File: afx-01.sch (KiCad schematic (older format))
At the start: 25 parts, among them P1 CONN_02X05, P2 CONN_02X08, Q5 BSS138, Q6 BSS138, U1 ADA_SSD1306_I2C, U10 MicroSD_Connector, U2 Teensy_3.1, U4 MicroSD_Adapter, U5 MCP1703

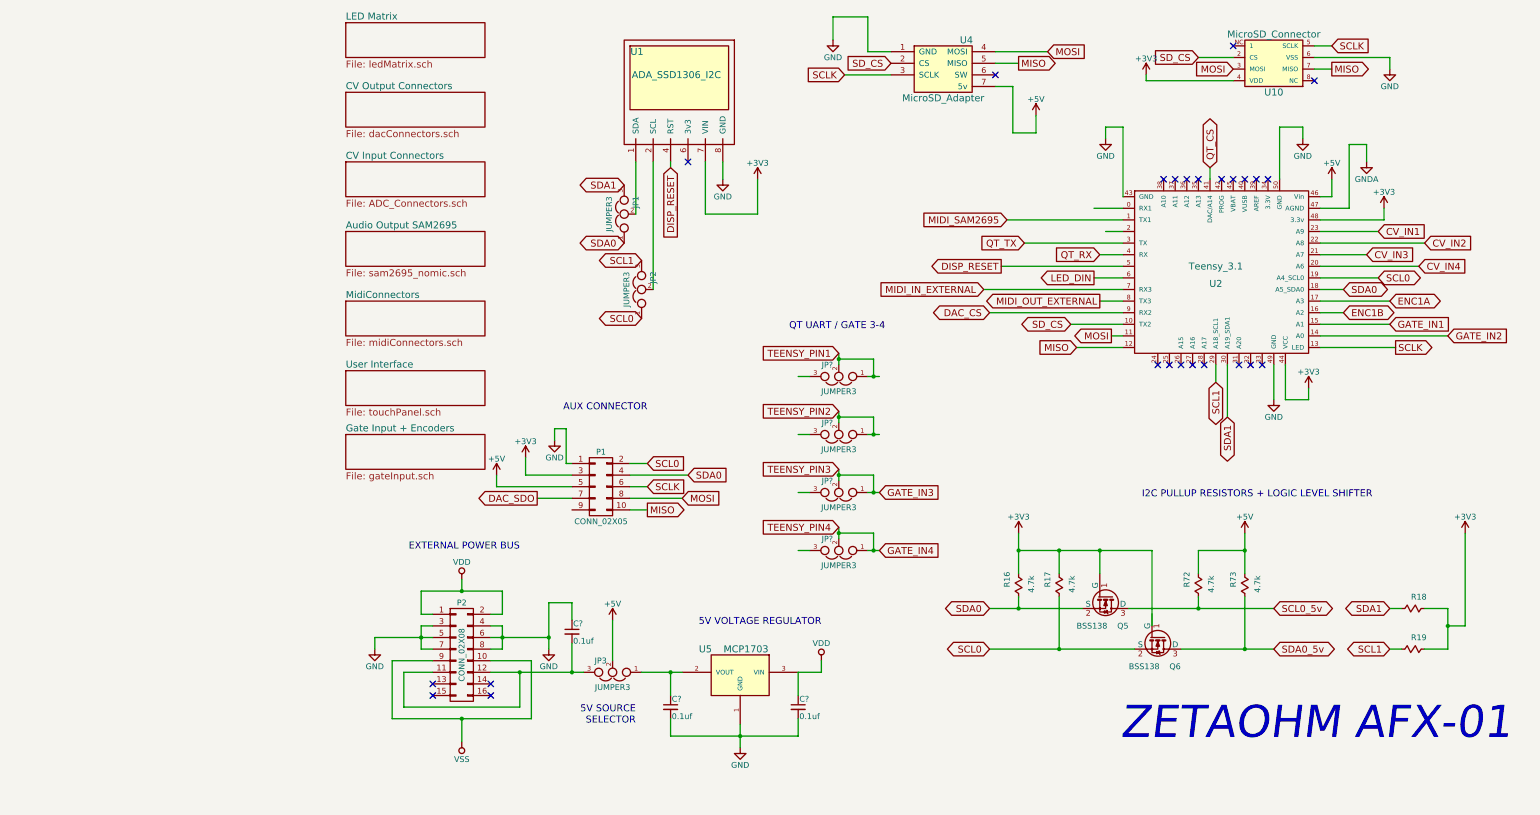
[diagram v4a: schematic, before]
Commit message: Updating footprints
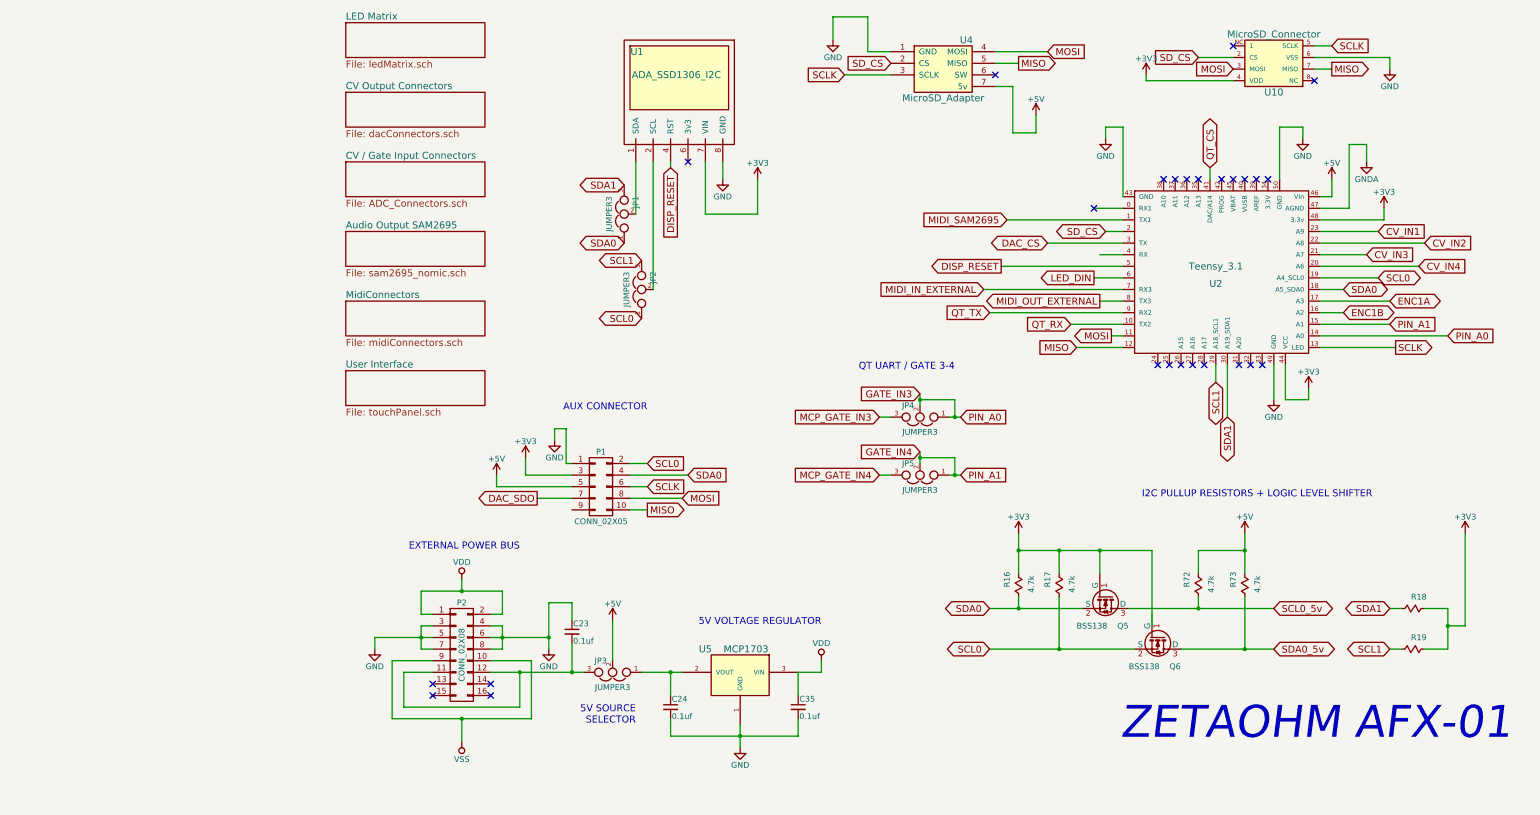
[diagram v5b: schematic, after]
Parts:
- removed JP? (x2): JUMPER3, Zetaohm:Jumper_3way, symbol JUMPER3
- C23, C24, C35: renamed from C?; footprint (none) -> Capacitors_SMD:C_0603_HandSoldering
- R16, R17, R18, R19, R72, R73: footprint Resistors_SMD:R_0805_HandSoldering -> Resistors_SMD:R_0603_HandSoldering
- U1: footprint Zetaohm:SSD1306 -> Pin_Headers:Pin_Header_Angled_1x06
- gave numbers to parts that had none: 2
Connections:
- net labels added: MCP_GATE_IN3, MCP_GATE_IN4, PIN_A0, PIN_A1
- net labels removed: GATE_IN1, GATE_IN2, TEENSY_PIN1, TEENSY_PIN2, TEENSY_PIN3, TEENSY_PIN4
- wire segments 168 -> 158
- no-connect marks 25 -> 26
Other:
- moved on the sheet: JP4, JP5
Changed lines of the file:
@@
 $Descr A4 11693 8268
 encoding utf-8
-Sheet 1 8
+Sheet 1 7
 Title ""
 Date ""
@@
 F 0 "R16" V 6900 5600 50  0000 C CNN
 F 1 "4.7k" V 6690 5640 50  0000 C CNN
-F 2 "Resistors_SMD:R_0805_HandSoldering" V 6730 5650 30  0001 C CNN
+F 2 "Resistors_SMD:R_0603_HandSoldering" V 6730 5650 30  0001 C CNN
 F 3 "" H 6800 5640 30  0000 C CNN
 	1    6800 5650
@@
 F 0 "R17" V 7250 5600 50  0000 C CNN
 F 1 "4.7k" V 7040 5640 50  0000 C CNN
-F 2 "Resistors_SMD:R_0805_HandSoldering" V 7080 5650 30  0001 C CNN
+F 2 "Resistors_SMD:R_0603_HandSoldering" V 7080 5650 30  0001 C CNN
 F 3 "" H 7150 5640 30  0000 C CNN
 	1    7150 5650
@@
 F 0 "R19" V 10300 6150 50  0000 C CNN
 F 1 "4.7k" V 10090 6190 50  0001 C CNN
-F 2 "Resistors_SMD:R_0805_HandSoldering" V 10130 6200 30  0001 C CNN
+F 2 "Resistors_SMD:R_0603_HandSoldering" V 10130 6200 30  0001 C CNN
 F 3 "" H 10200 6190 30  0000 C CNN
 	1    10200 6200
@@
 F 0 "R18" V 10300 5800 50  0000 C CNN
 F 1 "4.7k" V 10090 5840 50  0001 C CNN
-F 2 "Resistors_SMD:R_0805_HandSoldering" V 10130 5850 30  0001 C CNN
+F 2 "Resistors_SMD:R_0603_HandSoldering" V 10130 5850 30  0001 C CNN
 F 3 "" H 10200 5840 30  0000 C CNN
 	1    10200 5850
@@
 F 0 "U1" H 3510 2150 60  0000 C CNN
 F 1 "ADA_SSD1306_I2C" H 3850 1950 60  0000 C CNN
-F 2 "Zetaohm:SSD1306" V 4050 1550 60  0001 C CNN
+F 2 "Pin_Headers:Pin_Header_Angled_1x06" V 4050 1550 60  0001 C CNN
 F 3 "" V 4050 1550 60  0000 C CNN
 	1    3850 1600
@@
 	1    0    0    -1
 $EndComp
-Text GLabel 6550 3300 0    60   3State ~ 0
+Text GLabel 7050 2700 0    60   3State ~ 0
 DAC_CS
 Text GLabel 10050 3600 2    60   Output ~ 0
@@
 Text GLabel 7300 3600 0    60   Input ~ 0
 MISO
-Text GLabel 7250 3400 0    60   3State ~ 0
+Text GLabel 7550 2600 0    60   3State ~ 0
 SD_CS
 Text GLabel 5300 1250 0    60   Input ~ 0
@@
 S 1000 2000 1200 300
 U 561FE26C
-F0 "CV Input Connectors" 60
+F0 "CV / Gate Input Connectors" 60
 F1 "ADC_Connectors.sch" 60
 $EndSheet
@@
 Text GLabel 10250 2900 2    60   Input ~ 0
 CV_IN4
-Text GLabel 10000 3400 2    60   Input ~ 0
-GATE_IN1
-Text GLabel 10500 3500 2    60   Input ~ 0
-GATE_IN2
 NoConn ~ 8200 3750
 NoConn ~ 8100 3750
@@
 F 0 "R72" V 8450 5600 50  0000 C CNN
 F 1 "4.7k" V 8240 5640 50  0000 C CNN
-F 2 "Resistors_SMD:R_0805_HandSoldering" V 8280 5650 30  0001 C CNN
+F 2 "Resistors_SMD:R_0603_HandSoldering" V 8280 5650 30  0001 C CNN
 F 3 "" H 8350 5640 30  0000 C CNN
 	1    8350 5650
@@
 F 0 "R73" V 8850 5600 50  0000 C CNN
 F 1 "4.7k" V 8640 5640 50  0000 C CNN
-F 2 "Resistors_SMD:R_0805_HandSoldering" V 8680 5650 30  0001 C CNN
+F 2 "Resistors_SMD:R_0603_HandSoldering" V 8680 5650 30  0001 C CNN
 F 3 "" H 8750 5640 30  0000 C CNN
 	1    8750 5650
@@
 NoConn ~ 9350 1300
 $Comp
-L C_Small C?
+L C_Small C24
 U 1 1 5628B983
 P 3800 6700
-F 0 "C?" H 3810 6770 50  0000 L CNN
+F 0 "C24" H 3810 6770 50  0000 L CNN
 F 1 "0.1uf" H 3810 6620 50  0000 L CNN
-F 2 "" H 3800 6700 60  0000 C CNN
+F 2 "Capacitors_SMD:C_0603_HandSoldering" H 3800 6700 60  0001 C CNN
 F 3 "" H 3800 6700 60  0000 C CNN
 	1    3800 6700
@@
 $EndComp
 $Comp
-L C_Small C?
+L C_Small C35
 U 1 1 5628BCAF
 P 4900 6700
-F 0 "C?" H 4910 6770 50  0000 L CNN
+F 0 "C35" H 4910 6770 50  0000 L CNN
 F 1 "0.1uf" H 4910 6620 50  0000 L CNN
-F 2 "" H 4900 6700 60  0000 C CNN
+F 2 "Capacitors_SMD:C_0603_HandSoldering" H 4900 6700 60  0001 C CNN
 F 3 "" H 4900 6700 60  0000 C CNN
 	1    4900 6700
@@
 $EndComp
 $Comp
-L C_Small C?
+L C_Small C23
 U 1 1 5628C134
 P 2950 6050
-F 0 "C?" H 2960 6120 50  0000 L CNN
+F 0 "C23" H 2960 6120 50  0000 L CNN
 F 1 "0.1uf" H 2960 5970 50  0000 L CNN
-F 2 "" H 2950 6050 60  0000 C CNN
+F 2 "Capacitors_SMD:C_0603_HandSoldering" H 2950 6050 60  0001 C CNN
 F 3 "" H 2950 6050 60  0000 C CNN
 	1    2950 6050
@@
 Text GLabel 8450 2050 1    60   3State ~ 0
 QT_CS
-Text GLabel 5600 4850 2    60   Input ~ 0
+Text GLabel 5950 4000 0    60   Input ~ 0
 GATE_IN3
-Text GLabel 5600 5350 2    60   Input ~ 0
+Text GLabel 5950 4500 0    60   Input ~ 0
 GATE_IN4
-Text GLabel 7500 2800 0    60   Input ~ 0
+Text GLabel 7250 3400 0    60   Input ~ 0
 QT_RX
-Text GLabel 6850 2700 0    60   Input ~ 0
+Text GLabel 6550 3300 0    60   Input ~ 0
 QT_TX
 $Comp
-L JUMPER3 JP?
+L JUMPER3 JP4
 U 1 1 5629034F
-P 5250 4850
-F 0 "JP?" H 5300 4750 50  0000 L CNN
-F 1 "JUMPER3" H 5250 4950 50  0000 C BNN
-F 2 "Zetaohm:Jumper_3way" H 5250 4850 60  0001 C CNN
-F 3 "" H 5250 4850 60  0000 C CNN
-	1    5250 4850
+P 5950 4200
+F 0 "JP4" H 6000 4100 50  0000 L CNN
+F 1 "JUMPER3" H 5950 4300 50  0000 C BNN
+F 2 "Zetaohm:Jumper_3way" H 5950 4200 60  0001 C CNN
+F 3 "" H 5950 4200 60  0000 C CNN
+	1    5950 4200
 	-1   0    0    1
 $EndComp
 $Comp
-L JUMPER3 JP?
+L JUMPER3 JP5
 U 1 1 5629077E
-P 5250 5350
-F 0 "JP?" H 5300 5250 50  0000 L CNN
-F 1 "JUMPER3" H 5250 5450 50  0000 C BNN
-F 2 "Zetaohm:Jumper_3way" H 5250 5350 60  0001 C CNN
-F 3 "" H 5250 5350 60  0000 C CNN
-	1    5250 5350
+P 5950 4700
+F 0 "JP5" H 6000 4600 50  0000 L CNN
+F 1 "JUMPER3" H 5950 4800 50  0000 C BNN
+F 2 "Zetaohm:Jumper_3way" H 5950 4700 60  0001 C CNN
+F 3 "" H 5950 4700 60  0000 C CNN
+	1    5950 4700
 	-1   0    0    1
 $EndComp
-Text Notes 5650 3450 2    60   ~ 0
+Text Notes 6250 3800 2    60   ~ 0
 QT UART / GATE 3-4
-Text GLabel 5250 4650 0    60   Input ~ 0
-TEENSY_PIN3
-Text GLabel 5250 5150 0    60   Input ~ 0
-TEENSY_PIN4
-$Comp
-L JUMPER3 JP?
-U 1 1 562946F5
-P 5250 3850
-F 0 "JP?" H 5300 3750 50  0000 L CNN
-F 1 "JUMPER3" H 5250 3950 50  0000 C BNN
-F 2 "Zetaohm:Jumper_3way" H 5250 3850 60  0001 C CNN
-F 3 "" H 5250 3850 60  0000 C CNN
-	1    5250 3850
-	-1   0    0    1
-$EndComp
-$Comp
-L JUMPER3 JP?
-U 1 1 562946FB
-P 5250 4350
-F 0 "JP?" H 5300 4250 50  0000 L CNN
-F 1 "JUMPER3" H 5250 4450 50  0000 C BNN
-F 2 "Zetaohm:Jumper_3way" H 5250 4350 60  0001 C CNN
-F 3 "" H 5250 4350 60  0000 C CNN
-	1    5250 4350
-	-1   0    0    1
-$EndComp
-Text GLabel 5250 3650 0    60   Input ~ 0
-TEENSY_PIN1
-Text GLabel 5250 4150 0    60   Input ~ 0
-TEENSY_PIN2
 Wire Wire Line
 	9400 3200 10000 3200
@@
 	7550 2600 7700 2600
 Wire Wire Line
-	7700 2700 6850 2700
+	7700 2700 7050 2700
 Wire Wire Line
 	7500 2800 7700 2800
@@
 Connection ~ 2750 6100
 Wire Wire Line
-	4900 4850 5000 4850
-Wire Wire Line
-	5250 4650 5250 4750
-Wire Wire Line
-	5500 4850 5600 4850
-Wire Wire Line
-	5500 5350 5600 5350
-Wire Wire Line
-	5000 5350 4900 5350
-Wire Wire Line
-	5250 5150 5250 5250
-Wire Wire Line
-	4900 3850 5000 3850
-Wire Wire Line
-	5250 3650 5250 3750
-Wire Wire Line
-	5500 3850 5600 3850
-Wire Wire Line
-	5500 4350 5600 4350
-Wire Wire Line
-	5000 4350 4900 4350
-Wire Wire Line
-	5250 4150 5250 4250
-Wire Wire Line
-	5250 3700 5550 3700
-Wire Wire Line
-	5550 3700 5550 3850
-Connection ~ 5550 3850
-Connection ~ 5250 3700
-Wire Wire Line
-	5250 4200 5550 4200
-Wire Wire Line
-	5550 4200 5550 4350
-Connection ~ 5550 4350
-Connection ~ 5250 4200
-Wire Wire Line
-	5250 4700 5550 4700
-Wire Wire Line
-	5550 4700 5550 4850
-Connection ~ 5550 4850
-Connection ~ 5250 4700
-Wire Wire Line
-	5250 5200 5550 5200
-Wire Wire Line
-	5550 5200 5550 5350
-Connection ~ 5550 5350
-Connection ~ 5250 5200
-$Sheet
-S 1000 4350 1200 300
-U 56295FCA
-F0 "Gate Input + Encoders" 60
-F1 "gateInput.sch" 60
-$EndSheet
+	5600 4200 5700 4200
+Wire Wire Line
+	5950 4000 5950 4100
+Wire Wire Line
+	6200 4200 6300 4200
+Wire Wire Line
+	6200 4700 6300 4700
+Wire Wire Line
+	5700 4700 5600 4700
+Wire Wire Line
+	5950 4500 5950 4600
+Wire Wire Line
+	5950 4050 6250 4050
+Wire Wire Line
+	6250 4050 6250 4200
+Connection ~ 6250 4200
+Connection ~ 5950 4050
+Wire Wire Line
+	5950 4550 6250 4550
+Wire Wire Line
+	6250 4550 6250 4700
+Connection ~ 6250 4700
+Connection ~ 5950 4550
+Text GLabel 10000 3400 2    60   Input ~ 0
+PIN_A1
+Text GLabel 10500 3500 2    60   Input ~ 0
+PIN_A0
+Text GLabel 6300 4200 2    60   Input ~ 0
+PIN_A0
+Text GLabel 6300 4700 2    60   Input ~ 0
+PIN_A1
+Text GLabel 5600 4200 0    60   Input ~ 0
+MCP_GATE_IN3
+Text GLabel 5600 4700 0    60   Input ~ 0
+MCP_GATE_IN4
+NoConn ~ 7450 2400
 $EndSCHEMATC

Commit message: Populating pcb file
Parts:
- removed JP4, JP5: JUMPER3, Zetaohm:Jumper_3way, symbol JUMPER3
- P2: footprint Pin_Headers:Pin_Header_Angled_2x08 -> Pin_Headers:Pin_Header_Straight_2x08
- U1: footprint Pin_Headers:Pin_Header_Angled_1x06 -> Pin_Headers:Pin_Header_Straight_1x06
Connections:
- net GATE_IN3 renamed PIN_A0
- net GATE_IN4 renamed PIN_A1
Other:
- note removed: "QT UART / GATE 3-4"
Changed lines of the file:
@@
 F 0 "U1" H 3510 2150 60  0000 C CNN
 F 1 "ADA_SSD1306_I2C" H 3850 1950 60  0000 C CNN
-F 2 "Pin_Headers:Pin_Header_Angled_1x06" V 4050 1550 60  0001 C CNN
+F 2 "Pin_Headers:Pin_Header_Straight_1x06" V 4050 1550 60  0001 C CNN
 F 3 "" V 4050 1550 60  0000 C CNN
 	1    3850 1600
@@
 SD_CS
 $Comp
-L +3V3 #PWR01
+L +3V3 #PWR17
 U 1 1 561E6C12
 P 6800 5200
-F 0 "#PWR01" H 6800 5050 50  0001 C CNN
+F 0 "#PWR17" H 6800 5050 50  0001 C CNN
 F 1 "+3V3" H 6800 5340 50  0000 C CNN
 F 2 "" H 6800 5200 60  0000 C CNN
@@
 SCL1
 $Comp
-L +3V3 #PWR02
+L +3V3 #PWR19
 U 1 1 561E70C9
 P 10650 5200
-F 0 "#PWR02" H 10650 5050 50  0001 C CNN
+F 0 "#PWR19" H 10650 5050 50  0001 C CNN
 F 1 "+3V3" H 10650 5340 50  0000 C CNN
 F 2 "" H 10650 5200 60  0000 C CNN
@@
 ENC1B
 $Comp
-L +3V3 #PWR03
+L +3V3 #PWR12
 U 1 1 561E88DC
 P 9300 3950
-F 0 "#PWR03" H 9300 3800 50  0001 C CNN
+F 0 "#PWR12" H 9300 3800 50  0001 C CNN
 F 1 "+3V3" H 9300 4090 50  0000 C CNN
 F 2 "" H 9300 3950 60  0000 C CNN
@@
 $EndComp
 $Comp
-L GND #PWR04
+L GND #PWR13
 U 1 1 561E894C
 P 9000 4050
-F 0 "#PWR04" H 9000 3800 50  0001 C CNN
+F 0 "#PWR13" H 9000 3800 50  0001 C CNN
 F 1 "GND" H 9000 3900 50  0000 C CNN
 F 2 "" H 9000 4050 60  0000 C CNN
@@
 $EndComp
 $Comp
-L +5V #PWR05
+L +5V #PWR10
 U 1 1 561E8C0A
 P 9500 2150
-F 0 "#PWR05" H 9500 2000 50  0001 C CNN
+F 0 "#PWR10" H 9500 2000 50  0001 C CNN
 F 1 "+5V" H 9500 2290 50  0000 C CNN
 F 2 "" H 9500 2150 60  0000 C CNN
@@
 $EndComp
 $Comp
-L +3V3 #PWR06
+L +3V3 #PWR11
 U 1 1 561E8F33
 P 9950 2400
-F 0 "#PWR06" H 9950 2250 50  0001 C CNN
+F 0 "#PWR11" H 9950 2250 50  0001 C CNN
 F 1 "+3V3" H 9950 2540 50  0000 C CNN
 F 2 "" H 9950 2400 60  0000 C CNN
@@
 $EndComp
 $Comp
-L GNDA #PWR07
+L GNDA #PWR7
 U 1 1 561E8FA3
 P 9800 2000
-F 0 "#PWR07" H 9800 1750 50  0001 C CNN
+F 0 "#PWR7" H 9800 1750 50  0001 C CNN
 F 1 "GNDA" H 9800 1850 50  0000 C CNN
 F 2 "" H 9800 2000 60  0000 C CNN
@@
 SCLK
 $Comp
-L GND #PWR08
+L GND #PWR6
 U 1 1 561E9F99
 P 9250 1800
-F 0 "#PWR08" H 9250 1550 50  0001 C CNN
+F 0 "#PWR6" H 9250 1550 50  0001 C CNN
 F 1 "GND" H 9250 1650 50  0000 C CNN
 F 2 "" H 9250 1800 60  0000 C CNN
@@
 $EndComp
 $Comp
-L GND #PWR09
+L GND #PWR5
 U 1 1 561EA0E7
 P 7550 1800
-F 0 "#PWR09" H 7550 1550 50  0001 C CNN
+F 0 "#PWR5" H 7550 1550 50  0001 C CNN
 F 1 "GND" H 7550 1650 50  0000 C CNN
 F 2 "" H 7550 1800 60  0000 C CNN
@@
 SCLK
 $Comp
-L GND #PWR010
+L GND #PWR1
 U 1 1 561EAAFA
 P 5200 950
-F 0 "#PWR010" H 5200 700 50  0001 C CNN
+F 0 "#PWR1" H 5200 700 50  0001 C CNN
 F 1 "GND" H 5200 800 50  0000 C CNN
 F 2 "" H 5200 950 60  0000 C CNN
@@
 MOSI
 $Comp
-L +5V #PWR011
+L +5V #PWR4
 U 1 1 561EAD75
 P 6950 1600
-F 0 "#PWR011" H 6950 1450 50  0001 C CNN
+F 0 "#PWR4" H 6950 1450 50  0001 C CNN
 F 1 "+5V" H 6950 1740 50  0000 C CNN
 F 2 "" H 6950 1600 60  0000 C CNN
@@
 DISP_RESET
 $Comp
-L GND #PWR012
+L GND #PWR8
 U 1 1 561EB8E2
 P 4250 2150
-F 0 "#PWR012" H 4250 1900 50  0001 C CNN
+F 0 "#PWR8" H 4250 1900 50  0001 C CNN
 F 1 "GND" H 4250 2000 50  0000 C CNN
 F 2 "" H 4250 2150 60  0000 C CNN
@@
 $EndComp
 $Comp
-L +3V3 #PWR013
+L +3V3 #PWR9
 U 1 1 561EBA2E
 P 4550 2150
-F 0 "#PWR013" H 4550 2000 50  0001 C CNN
+F 0 "#PWR9" H 4550 2000 50  0001 C CNN
 F 1 "+3V3" H 4550 2290 50  0000 C CNN
 F 2 "" H 4550 2150 60  0000 C CNN
@@
 LED_DIN
 $Comp
-L GND #PWR014
+L GND #PWR14
 U 1 1 561EC8D9
 P 2800 4400
-F 0 "#PWR014" H 2800 4150 50  0001 C CNN
+F 0 "#PWR14" H 2800 4150 50  0001 C CNN
 F 1 "GND" H 2800 4250 50  0000 C CNN
 F 2 "" H 2800 4400 60  0000 C CNN
@@
 $EndComp
 $Comp
-L +3V3 #PWR015
+L +3V3 #PWR15
 U 1 1 561EC92C
 P 2550 4550
-F 0 "#PWR015" H 2550 4400 50  0001 C CNN
+F 0 "#PWR15" H 2550 4400 50  0001 C CNN
 F 1 "+3V3" H 2550 4690 50  0000 C CNN
 F 2 "" H 2550 4550 60  0000 C CNN
@@
 $EndComp
 $Comp
-L +5V #PWR016
+L +5V #PWR16
 U 1 1 561EC97F
 P 2300 4700
-F 0 "#PWR016" H 2300 4550 50  0001 C CNN
+F 0 "#PWR16" H 2300 4550 50  0001 C CNN
 F 1 "+5V" H 2300 4840 50  0000 C CNN
 F 2 "" H 2300 4700 60  0000 C CNN
@@
 SCLK
 $Comp
-L VDD #PWR017
+L VDD #PWR20
 U 1 1 561ED246
 P 2000 5600
-F 0 "#PWR017" H 2000 5450 50  0001 C CNN
+F 0 "#PWR20" H 2000 5450 50  0001 C CNN
 F 1 "VDD" H 2000 5750 50  0000 C CNN
 F 2 "" H 2000 5600 60  0000 C CNN
@@
 $EndComp
 $Comp
-L VSS #PWR018
+L VSS #PWR25
 U 1 1 561ED2BD
 P 2000 7000
-F 0 "#PWR018" H 2000 6850 50  0001 C CNN
+F 0 "#PWR25" H 2000 6850 50  0001 C CNN
 F 1 "VSS" H 2000 7150 50  0000 C CNN
 F 2 "" H 2000 7000 60  0000 C CNN
@@
 $EndComp
 $Comp
-L GND #PWR019
+L GND #PWR22
 U 1 1 561ED883
 P 1250 6200
-F 0 "#PWR019" H 1250 5950 50  0001 C CNN
+F 0 "#PWR22" H 1250 5950 50  0001 C CNN
 F 1 "GND" H 1250 6050 50  0000 C CNN
 F 2 "" H 1250 6200 60  0000 C CNN
@@
 $EndComp
 $Comp
-L GND #PWR020
+L GND #PWR23
 U 1 1 561ED8D9
 P 2750 6200
-F 0 "#PWR020" H 2750 5950 50  0001 C CNN
+F 0 "#PWR23" H 2750 5950 50  0001 C CNN
 F 1 "GND" H 2750 6050 50  0000 C CNN
 F 2 "" H 2750 6200 60  0000 C CNN
@@
 $EndComp
 $Comp
-L GND #PWR021
+L GND #PWR26
 U 1 1 5620975C
 P 4400 7050
-F 0 "#PWR021" H 4400 6800 50  0001 C CNN
+F 0 "#PWR26" H 4400 6800 50  0001 C CNN
 F 1 "GND" H 4400 6900 50  0000 C CNN
 F 2 "" H 4400 7050 60  0000 C CNN
@@
 $EndComp
 $Comp
-L VDD #PWR022
+L VDD #PWR24
 U 1 1 562097B5
 P 5100 6300
-F 0 "#PWR022" H 5100 6150 50  0001 C CNN
+F 0 "#PWR24" H 5100 6150 50  0001 C CNN
 F 1 "VDD" H 5100 6450 50  0000 C CNN
 F 2 "" H 5100 6300 60  0000 C CNN
@@
 $EndComp
 $Comp
-L +5V #PWR023
+L +5V #PWR21
 U 1 1 5620980E
 P 3300 5950
-F 0 "#PWR023" H 3300 5800 50  0001 C CNN
+F 0 "#PWR21" H 3300 5800 50  0001 C CNN
 F 1 "+5V" H 3300 6090 50  0000 C CNN
 F 2 "" H 3300 5950 60  0000 C CNN
@@
 $EndComp
 $Comp
-L +5V #PWR024
+L +5V #PWR18
 U 1 1 56228B3B
 P 8750 5200
-F 0 "#PWR024" H 8750 5050 50  0001 C CNN
+F 0 "#PWR18" H 8750 5050 50  0001 C CNN
 F 1 "+5V" H 8750 5340 50  0000 C CNN
 F 2 "" H 8750 5200 60  0000 C CNN
@@
 F 0 "P2" H 2000 6700 50  0000 C CNN
 F 1 "CONN_02X08" V 2000 6250 50  0000 C CNN
-F 2 "Pin_Headers:Pin_Header_Angled_2x08" H 2000 5050 60  0001 C CNN
+F 2 "Pin_Headers:Pin_Header_Straight_2x08" H 2000 5050 60  0001 C CNN
 F 3 "" H 2000 5050 60  0000 C CNN
 	1    2000 6250
@@
 SCLK
 $Comp
-L +3V3 #PWR025
+L +3V3 #PWR3
 U 1 1 56235638
 P 7900 1250
-F 0 "#PWR025" H 7900 1100 50  0001 C CNN
+F 0 "#PWR3" H 7900 1100 50  0001 C CNN
 F 1 "+3V3" H 7900 1390 50  0000 C CNN
 F 2 "" H 7900 1250 60  0000 C CNN
@@
 $EndComp
 $Comp
-L GND #PWR026
+L GND #PWR2
 U 1 1 562356B5
 P 10000 1200
-F 0 "#PWR026" H 10000 950 50  0001 C CNN
+F 0 "#PWR2" H 10000 950 50  0001 C CNN
 F 1 "GND" H 10000 1050 50  0000 C CNN
 F 2 "" H 10000 1200 60  0000 C CNN
@@
 Text GLabel 8450 2050 1    60   3State ~ 0
 QT_CS
-Text GLabel 5950 4000 0    60   Input ~ 0
-GATE_IN3
-Text GLabel 5950 4500 0    60   Input ~ 0
-GATE_IN4
 Text GLabel 7250 3400 0    60   Input ~ 0
 QT_RX
 Text GLabel 6550 3300 0    60   Input ~ 0
 QT_TX
-$Comp
-L JUMPER3 JP4
-U 1 1 5629034F
-P 5950 4200
-F 0 "JP4" H 6000 4100 50  0000 L CNN
-F 1 "JUMPER3" H 5950 4300 50  0000 C BNN
-F 2 "Zetaohm:Jumper_3way" H 5950 4200 60  0001 C CNN
-F 3 "" H 5950 4200 60  0000 C CNN
-	1    5950 4200
-	-1   0    0    1
-$EndComp
-$Comp
-L JUMPER3 JP5
-U 1 1 5629077E
-P 5950 4700
-F 0 "JP5" H 6000 4600 50  0000 L CNN
-F 1 "JUMPER3" H 5950 4800 50  0000 C BNN
-F 2 "Zetaohm:Jumper_3way" H 5950 4700 60  0001 C CNN
-F 3 "" H 5950 4700 60  0000 C CNN
-	1    5950 4700
-	-1   0    0    1
-$EndComp
-Text Notes 6250 3800 2    60   ~ 0
-QT UART / GATE 3-4
 Wire Wire Line
 	9400 3200 10000 3200
@@
 	2950 5800 2950 5950
 Connection ~ 2750 6100
-Wire Wire Line
-	5600 4200 5700 4200
-Wire Wire Line
-	5950 4000 5950 4100
-Wire Wire Line
-	6200 4200 6300 4200
-Wire Wire Line
-	6200 4700 6300 4700
-Wire Wire Line
-	5700 4700 5600 4700
-Wire Wire Line
-	5950 4500 5950 4600
-Wire Wire Line
-	5950 4050 6250 4050
-Wire Wire Line
-	6250 4050 6250 4200
-Connection ~ 6250 4200
-Connection ~ 5950 4050
-Wire Wire Line
-	5950 4550 6250 4550
-Wire Wire Line
-	6250 4550 6250 4700
-Connection ~ 6250 4700
-Connection ~ 5950 4550
 Text GLabel 10000 3400 2    60   Input ~ 0
 PIN_A1
 Text GLabel 10500 3500 2    60   Input ~ 0
 PIN_A0
-Text GLabel 6300 4200 2    60   Input ~ 0
-PIN_A0
-Text GLabel 6300 4700 2    60   Input ~ 0
-PIN_A1
-Text GLabel 5600 4200 0    60   Input ~ 0
-MCP_GATE_IN3
-Text GLabel 5600 4700 0    60   Input ~ 0
-MCP_GATE_IN4
 NoConn ~ 7450 2400
 $EndSCHEMATC
